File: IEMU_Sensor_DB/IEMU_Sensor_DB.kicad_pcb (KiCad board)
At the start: 2 copper layers, 51 x 29 mm, 12 parts, among them J1 USB_C_Receptacle_USB2.0_16P, J2 Conn_ARM_SWD_TagConnect_TC203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, J3 503398-1892, Q1 CSD85301Q2, U1 Ezurio BL54L15, U2 BQ29702DSER, U3 NPM1304-QEAA-R7, U4 USBLC6-2P6, U5 LSM6DSV320XTR, U6 MMC5603NJ

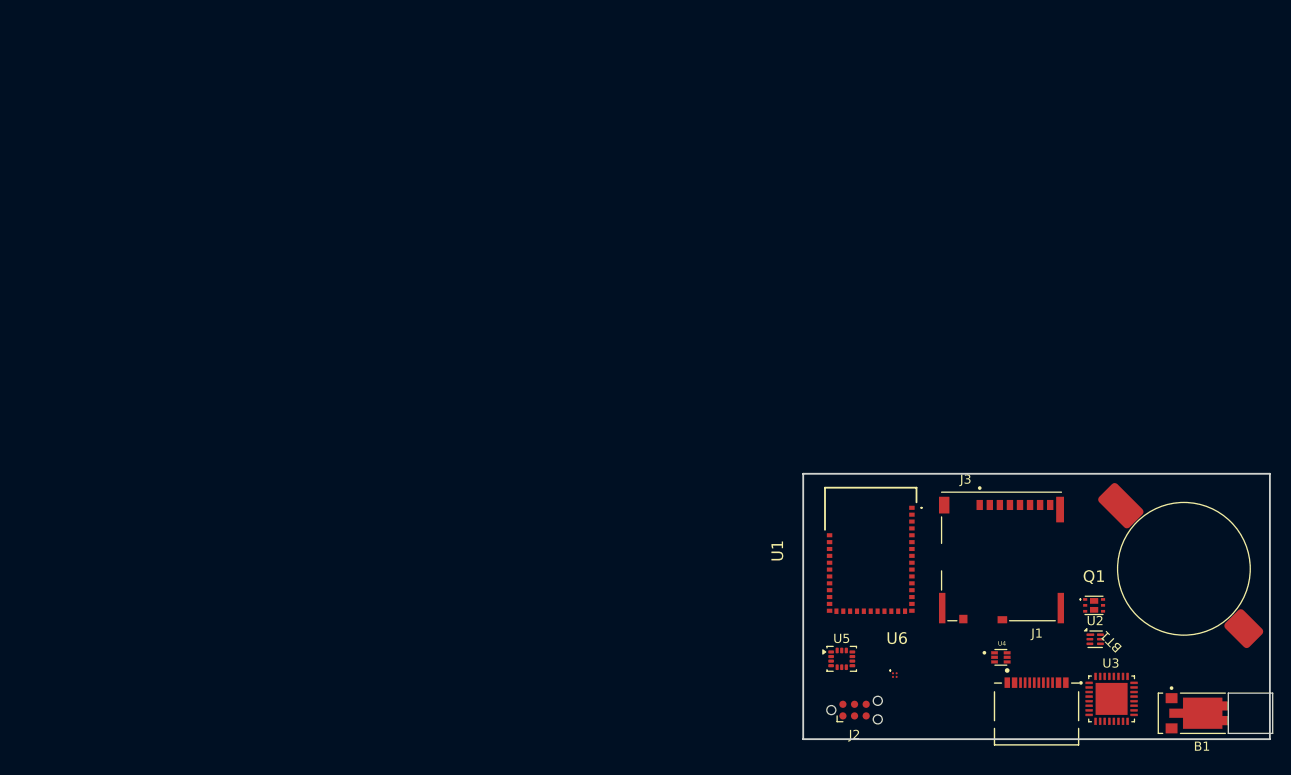
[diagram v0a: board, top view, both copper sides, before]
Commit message: created the layout for the sensor (not finished)
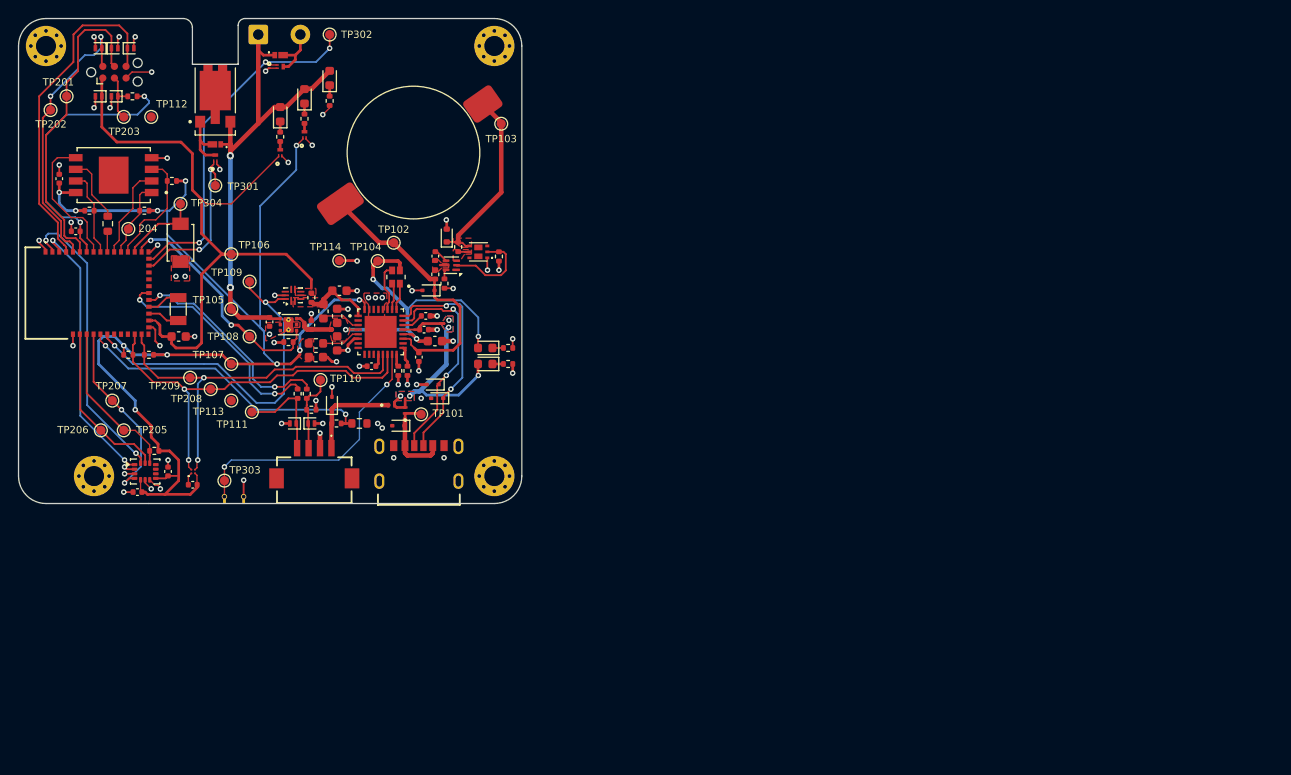
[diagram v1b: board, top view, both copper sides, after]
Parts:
- removed B1: VZ43FM1B8230001L, 0_Feedback:XDCR_VZ43FM1B8230001L
- removed BT1: Battery_Cell, 0_Power:CoinCell_LIR1455_LBY2
- removed J1: USB_C_Receptacle_USB2.0_16P, 0_Connectors:CONN_8p94X6p5X3p16_12L_GCC
- removed J2: Conn_ARM_SWD_TagConnect_TC2030-NL, Connector:Tag-Connect_TC2030-IDC-NL_2x03_P1.27mm_Vertical
- removed J3: 503398-1892, 0_Connectors:MOLEX_503398-1892
- removed Q1: CSD85301Q2, 0_Power:CSD85301Q2
- removed U1: Ezurio BL54L15, 0_MCU:BL54L15
- removed U2: BQ29702DSER, Package_SON:WSON-6_1.5x1.5mm_P0.5mm
- removed U3: NPM1304-QEAA-R7, 0_Power:QFN50P500X500X90-33N
- removed U4: USBLC6-2P6, 0_Power:SOT50P160X60-6N
- removed U5: LSM6DSV320XTR, Package_LGA:LGA-14_3x2.5mm_P0.5mm_LayoutBorder3x4y
- removed U6: MMC5603NJ, 0_Sensors:MMC5603NJ
- added 204: ~, TestPoint:TestPoint_Pad_D1.0mm, F.Cu at (101.2, 81.2)
- added BT101: Battery_Cell, 0_Power:CoinCell_LIR1455_LBY2, F.Cu at (138.6, 81.7)
- added C101: 1u, Capacitor_SMD:C_0402_1005Metric, F.Cu at (133.6, 92.2)
- added C102: 2u2, Capacitor_SMD:C_0402_1005Metric, F.Cu at (133.0, 95.2)
- added C103: 100n, Capacitor_SMD:C_0402_1005Metric, F.Cu at (134.8, 84.2)
- added C104: 100n, Capacitor_SMD:C_0402_1005Metric, F.Cu at (127.8, 96.2)
- added C105: 1u, Capacitor_SMD:C_0402_1005Metric, F.Cu at (133.8, 90.8)
- added C106: 10u, Capacitor_SMD:C_0603_1608Metric, F.Cu at (134.8, 93.5)
- added C107: 10u, Capacitor_SMD:C_0603_1608Metric, F.Cu at (124.1, 90.7)
- added C108: 10u, Capacitor_SMD:C_0603_1608Metric, F.Cu at (124.1, 93.7)
- added C109: 1u, Capacitor_SMD:C_0402_1005Metric, F.Cu at (121.2, 91.8)
- added C110: 1u, Capacitor_SMD:C_0402_1005Metric, F.Cu at (116.7, 91.4)
- added C111: 10u, Capacitor_SMD:C_0603_1608Metric, F.Cu at (124.3, 88.0)
- added C112: 10u, Capacitor_SMD:C_0603_1608Metric, F.Cu at (121.8, 95.2)
- added C201: 10u, Capacitor_SMD:C_0603_1608Metric, F.Cu at (106.8, 93.0)
- added C202: 3p7, Capacitor_SMD:C_0402_1005Metric, F.Cu at (95.5, 81.5)
- added C203: 100n, Capacitor_SMD:C_0402_1005Metric, F.Cu at (93.7, 75.8)
- added C204: 100n, Capacitor_SMD:C_0402_1005Metric, F.Cu at (105.6, 107.8)
- added C205: 100n, Capacitor_SMD:C_0402_1005Metric, F.Cu at (102.2, 110.0)
- added C206: 2u2, Capacitor_SMD:C_0402_1005Metric, F.Cu at (108.3, 109.2)
- added D101: ESD5Z5.0T1G, Diode_SMD:D_SOD-523_1, F.Cu at (130.8, 102.8)
- added D102: ESD5Z5.0T1G, Diode_SMD:D_SOD-523_1, F.Cu at (134.5, 98.2)
- added D103: ESD5Z5.0T1G, Diode_SMD:D_SOD-523_1, F.Cu at (135.0, 99.8)
- added D104: PMEG3010ESBYL, 0_Power:DIODFN100X60X30-2N, F.Cu at (131.5, 101.1)
- added D105: PMEG3010ESBYL, 0_Power:DIODFN100X60X30-2N, F.Cu at (130.0, 100.5)
- added D106: ESD5Z5.0T1G, Diode_SMD:D_SOD-523_1, F.Cu at (123.5, 100.2)
- added D107: ESD9L1P8, Diode_SMD:D_SOD-882, F.Cu at (119.2, 102.5)
- added D108: ESD9L1P8, Diode_SMD:D_SOD-882, F.Cu at (121.2, 102.5)
- added D109: LTST-C19HE1WT, 0_Feedback:LED_LTST-C19HE1WT, F.Cu at (130.5, 86.5)
- added D110: ESD5Z5.0T1G, Diode_SMD:D_SOD-523_1, F.Cu at (134.0, 88.0)
- added D111: TPD1E10B06DYAR, Diode_SMD:D_SOD-523, F.Cu at (136.0, 82.0)
- added D201: ESD9L1P8, Diode_SMD:D_SOD-882, F.Cu at (99.8, 61.5)
- added D202: ESD9L1P8, Diode_SMD:D_SOD-882, F.Cu at (98.0, 61.5)
- added D203: ESD9L1P8, Diode_SMD:D_SOD-882, F.Cu at (101.5, 61.5)
- added D204: ESD9L1P8, Diode_SMD:D_SOD-882, F.Cu at (99.8, 66.8)
- added D205: ESD9L1P8, Diode_SMD:D_SOD-882, F.Cu at (98.0, 66.8)
- added D301: D_Schottky_2A_40V_0603, 0_Power:0603_DSN, F.Cu at (110.8, 72.0)
- added D302: D_Schottky_2A_40V_0603, 0_Power:0603_DSN, F.Cu at (117.8, 62.2)
- added D303: LTST-C191KRKT, 0_Feedback:LTST-C191KRKT, F.Cu at (117.8, 68.7)
- added D304: LTST-C191KRKT, 0_Feedback:LTST-C191KRKT, F.Cu at (120.5, 66.8)
- added D305: LTST-C191KRKT, 0_Feedback:LTST-C191KRKT, F.Cu at (123.2, 64.8)
- added D306: LTST-C191KRKT, 0_Feedback:LTST-C191KRKT, F.Cu at (140.2, 96.0)
- added D307: LTST-C191KRKT, 0_Feedback:LTST-C191KRKT, F.Cu at (140.2, 94.2)
- added J101: USB4125-GF-A, 0_Connectors:GCT_USB4125-GF-A_REVA2, F.Cu at (133.0, 108.0)
- added J102: DF13-4P-1.25H(21), 0_Connectors:DF13-4P-1.25H(21), F.Cu at (121.6, 108.7)
- added J201: Conn_ARM_SWD_TagConnect_TC2030-NL, Connector:Tag-Connect_TC2030-IDC-NL_2x03_P1.27mm_Vertical, F.Cu at (99.7, 64.1)
- added J301: Conn_01x02_Pin, Connector_Wire:SolderWire-0.5sqmm_1x02_P4.6mm_D0.9mm_OD2.1mm, F.Cu at (115.5, 60.0)
- added L101: 2u2, Inductor_SMD:L_0603_1608Metric, F.Cu at (122.6, 90.2)
- added L102: 2u2, Inductor_SMD:L_0603_1608Metric, F.Cu at (121.8, 93.8)
- added M401: VZ43FM1B8230001L, 0_Feedback:XDCR_VZ43FM1B8230001L, F.Cu at (110.8, 67.0)
- added MH301: MountingHole_Pad, MountingHole:MountingHole_2.2mm_M2_Pad_Via, F.Cu at (97.5, 108.2)
- added MH302: MountingHole_Pad, MountingHole:MountingHole_2.2mm_M2_Pad_Via, F.Cu at (92.2, 61.2)
- added MH303: MountingHole_Pad, MountingHole:MountingHole_2.2mm_M2_Pad_Via, F.Cu at (141.2, 61.2)
- added MH304: MountingHole_Pad, MountingHole:MountingHole_2.2mm_M2_Pad_Via, F.Cu at (141.2, 108.2)
- added Q101: CSD85301Q2, 0_Power:CSD85301Q2, F.Cu at (139.5, 83.8)
- added Q301: CSD13381F4, 0_Power:DFN100X60X35-3N, F.Cu at (110.8, 73.5)
- added Q302: CSD13381F4, 0_Power:DFN100X60X35-3N, F.Cu at (117.8, 63.5)
- added Q303: CSD13381F4, 0_Power:DFN100X60X35-3N, F.Cu at (117.8, 72.9)
- added Q304: CSD13381F4, 0_Power:DFN100X60X35-3N, F.Cu at (120.5, 71.0)
- added R101: 10k, Resistor_SMD:R_0402_1005Metric, F.Cu at (121.2, 101.0)
- added R102: 47k, Resistor_SMD:R_0402_1005Metric, F.Cu at (131.8, 96.8)
- added R103: 47k, Resistor_SMD:R_0402_1005Metric, F.Cu at (130.8, 96.8)
- added R104: 330, Resistor_SMD:R_0402_1005Metric, F.Cu at (134.8, 86.2)
- added R105: 5M1, Resistor_SMD:R_0402_1005Metric, F.Cu at (137.3, 83.2)
- added R106: 5M1, Resistor_SMD:R_0402_1005Metric, F.Cu at (141.8, 84.2)
- added R107: 2k2, Resistor_SMD:R_0402_1005Metric, F.Cu at (135.8, 87.2)
- added R108: R_Shunt_1R, Resistor_SMD:R_0402_1005Metric, F.Cu at (121.2, 88.8)
- added R109: 1k, Resistor_SMD:R_0402_1005Metric, F.Cu at (119.8, 99.2)
- added R110: 1k, Resistor_SMD:R_0402_1005Metric, F.Cu at (120.8, 99.2)
- added R111: 510k, Resistor_SMD:R_0603_1608Metric, F.Cu at (126.5, 102.5)
- added R112: 1M, Resistor_SMD:R_0402_1005Metric, F.Cu at (124.0, 102.5)
- added R201: 1k, Resistor_SMD:R_0402_1005Metric, F.Cu at (101.7, 66.8)
- added R202: 22R, Resistor_SMD:R_0603_1608Metric, F.Cu at (99.0, 80.7)
- added R203: 47k, Resistor_SMD:R_0402_1005Metric, F.Cu at (97.0, 79.2)
- added R204: 47k, Resistor_SMD:R_0402_1005Metric, F.Cu at (106.0, 76.0)
- added R205: 47k, Resistor_SMD:R_0402_1005Metric, F.Cu at (103.0, 79.2)
- added R206: 10k, Resistor_SMD:R_0402_1005Metric, F.Cu at (104.1, 105.5)
- added R207: 2k2, Resistor_SMD:R_0402_1005Metric, F.Cu at (103.5, 95.0)
- added R208: 2k2, Resistor_SMD:R_0402_1005Metric, F.Cu at (101.2, 95.0)
- added R209: 1M, Resistor_SMD:R_0402_1005Metric, F.Cu at (118.8, 93.6)
- added R301: 330R, Resistor_SMD:R_0402_1005Metric, F.Cu at (117.8, 71.2)
- added R302: 330R, Resistor_SMD:R_0402_1005Metric, F.Cu at (120.5, 69.2)
- added R303: 330R, Resistor_SMD:R_0402_1005Metric, F.Cu at (123.2, 67.2)
- added R304: 1k, Resistor_SMD:R_0402_1005Metric, F.Cu at (142.8, 96.0)
- added R305: 1k, Resistor_SMD:R_0402_1005Metric, F.Cu at (142.8, 94.2)
- added SW301: NANOT_160_BP, 0_Feedback:NANOT160BP, F.Cu at (112.8, 111.0)
- added SW302: TS-1088-AR02016, 0_Feedback:SW_TS-1088-AR02016, F.Cu at (107.0, 82.8)
- added TP101: ~, TestPoint:TestPoint_Pad_D1.0mm, F.Cu at (133.2, 101.5)
- added TP102: ~, TestPoint:TestPoint_Pad_D1.0mm, F.Cu at (130.2, 82.8)
- added TP103: ~, TestPoint:TestPoint_Pad_D1.0mm, F.Cu at (142.0, 69.8)
- added TP104: ~, TestPoint:TestPoint_Pad_D1.0mm, F.Cu at (128.5, 84.8)
- added TP105: ~, TestPoint:TestPoint_Pad_D1.0mm, F.Cu at (112.5, 90.0)
- added TP106: ~, TestPoint:TestPoint_Pad_D1.0mm, F.Cu at (112.5, 84.0)
- added TP107: ~, TestPoint:TestPoint_Pad_D1.0mm, F.Cu at (112.5, 96.0)
- added TP108: ~, TestPoint:TestPoint_Pad_D1.0mm, F.Cu at (114.5, 93.0)
- added TP109: ~, TestPoint:TestPoint_Pad_D1.0mm, F.Cu at (114.5, 87.0)
- added TP110: ~, TestPoint:TestPoint_Pad_D1.0mm, F.Cu at (122.2, 97.8)
- added TP111: ~, TestPoint:TestPoint_Pad_D1.0mm, F.Cu at (114.8, 101.2)
- added TP112: ~, TestPoint:TestPoint_Pad_D1.0mm, F.Cu at (103.8, 69.0)
- added TP113: ~, TestPoint:TestPoint_Pad_D1.0mm, F.Cu at (112.5, 100.0)
- added TP114: ~, TestPoint:TestPoint_Pad_D1.0mm, F.Cu at (124.3, 84.7)
- added TP201: ~, TestPoint:TestPoint_Pad_D1.0mm, F.Cu at (94.5, 66.8)
- added TP202: ~, TestPoint:TestPoint_Pad_D1.0mm, F.Cu at (92.8, 68.2)
- added TP203: ~, TestPoint:TestPoint_Pad_D1.0mm, F.Cu at (100.8, 69.0)
- added TP205: ~, TestPoint:TestPoint_Pad_D1.0mm, F.Cu at (100.8, 103.2)
- added TP206: ~, TestPoint:TestPoint_Pad_D1.0mm, F.Cu at (98.2, 103.2)
- added TP207: ~, TestPoint:TestPoint_Pad_D1.0mm, F.Cu at (99.5, 100.0)
- added TP208: ~, TestPoint:TestPoint_Pad_D1.0mm, F.Cu at (110.2, 98.8)
- added TP209: ~, TestPoint:TestPoint_Pad_D1.0mm, F.Cu at (108.0, 97.5)
- added TP301: ~, TestPoint:TestPoint_Pad_D1.0mm, F.Cu at (110.8, 76.5)
- added TP302: ~, TestPoint:TestPoint_Pad_D1.0mm, F.Cu at (123.2, 60.0)
- added TP303: ~, TestPoint:TestPoint_Pad_D1.0mm, F.Cu at (111.8, 108.8)
- added TP304: ~, TestPoint:TestPoint_Pad_D1.0mm, F.Cu at (107.0, 78.5)
- added U101: NPM1304-QEAA-R7, 0_Power:QFN50P500X500X90-33N, F.Cu at (128.8, 92.5)
- added U102: BQ29702DSER, Package_SON:WSON-6_1.5x1.5mm_P0.5mm, F.Cu at (136.5, 85.2)
- added U103: TLV75530PDRVR, Package_SON:WSON-6-1EP_2x2mm_P0.65mm_EP1x1.6mm_ThermalVias, F.Cu at (118.8, 91.7)
- added U104: INA216A2RSWR, Package_DFN_QFN:Texas_RSW0010A_UQFN-10_1.4x1.8mm_P0.4mm, F.Cu at (119.2, 88.5)
- added U201: Ezurio BL54L15, 0_MCU:BL54L15, F.Cu at (97.0, 88.2)
- added U202: W25N02JWZEIF, 0_Memory:IC_W25N04KVZEIR, F.Cu at (99.7, 75.4)
- added U203: LSM6DSV320XTR, Package_LGA:LGA-14_3x2.5mm_P0.5mm_LayoutBorder3x4y, F.Cu at (103.1, 107.8)
- added U204: MMC5603NJ, 0_Sensors:MMC5603NJ, F.Cu at (108.3, 107.8)
- added Y201: 32.768kHz, Crystal:Crystal_SMD_3215-2Pin_3.2x1.5mm, F.Cu at (106.7, 90.0)
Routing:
- net +1V8_Peripherals: track 0.00 -> 140.5 mm, vias 0 -> 11
- net +1V8_MCU: track 0.00 -> 70.8 mm
- net GND: track 0.00 -> 70.6 mm, vias 0 -> 64
- net +3V0: track 0.00 -> 55.3 mm, vias 0 -> 2
- net /1_Power/NPM_SCL: track 0.00 -> 44.8 mm, vias 0 -> 2
- net /1_Power/NPM_SDA: track 0.00 -> 43.3 mm, vias 0 -> 2
- net +VSYS: track 0.00 -> 43.0 mm, vias 0 -> 4
- net /2_nRF Module & NAND Flash + IMU + Magnetometer/ACTUATOR_EXTERNAL_EN: track 0.00 -> 39.5 mm, vias 0 -> 3
- net /1_Power/MCU_CURR_MON_COMP: track 0.00 -> 39.3 mm, vias 0 -> 2
- net /2_nRF Module & NAND Flash + IMU + Magnetometer/SWD_O: track 0.00 -> 36.9 mm
- net /2_nRF Module & NAND Flash + IMU + Magnetometer/SWD_CLK: track 0.00 -> 34.8 mm
- net /1_Power/5V_CHG_DET: track 0.00 -> 33.0 mm, vias 0 -> 2
- net /2_nRF Module & NAND Flash + IMU + Magnetometer/SPI_MISO_IMU: track 0.00 -> 32.4 mm, vias 0 -> 2
- net /2_nRF Module & NAND Flash + IMU + Magnetometer/SWD_IO: track 0.00 -> 31.4 mm, vias 0 -> 2
- net +VBAT: track 0.00 -> 30.4 mm
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- added copper zone on F.Cu, net +1V8_MCU
- added copper zone on F.Cu, net +1V8_Peripherals
- added copper zone on B.Cu, net +VBUS_IN
- added copper zone on F.Cu, net +VBUS_IN
- added copper zone on F.Cu, net +VSYS
- added copper zone on F.Cu, net /1_Power/BAT-
- added copper zone on F.Cu, net /1_Power/BAT_P_BAT
- added copper zone on F.Cu, net /1_Power/BAT_P_DOUT
- added copper zone on F.Cu, net /1_Power/NPM_VOUT1
- added copper zone on F.Cu, net GND
- added copper zone on In1.Cu, net GND
- added copper zone on In2.Cu, net GND
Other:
- board size 51 x 29 mm -> 55 x 53 mm
- copper layers 2 -> 4
- rule pad_to_mask_clearance: 0 -> 0.05

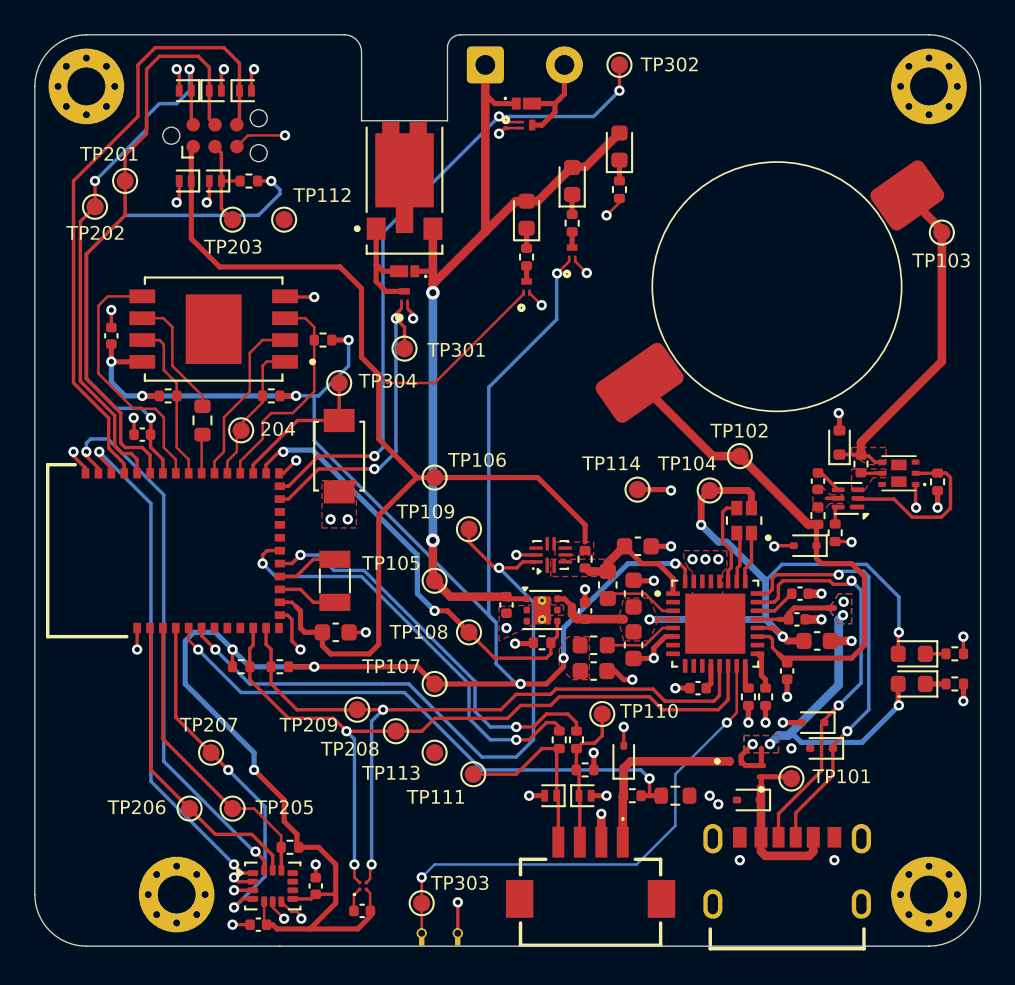
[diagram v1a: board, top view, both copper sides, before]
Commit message: finished layout for sensor
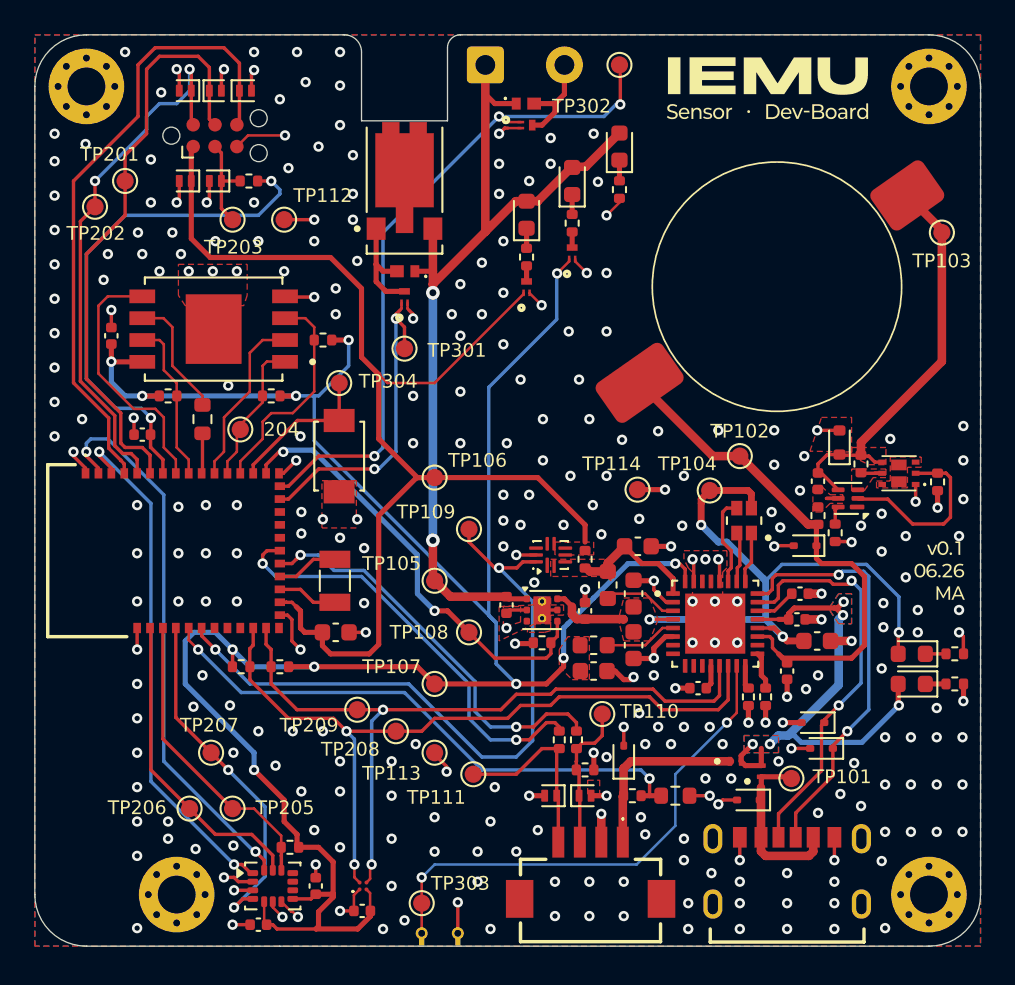
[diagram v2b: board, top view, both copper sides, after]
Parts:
- moved R202 0.08 mm to (99.0, 80.6)
- moved 204 0.07 mm to (101.2, 81.2)
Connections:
- net Net-(Q101-D1_1) renamed /1_Power/BAT_FET
- R202 pad 1: /2_nRF Module & NAND Flash + IMU + Magnetometer/QSPI_CLK -> /2_nRF Module & NAND Flash + IMU + Magnetometer/QSPI_CLK_MCU
- U201 pad 10: /2_nRF Module & NAND Flash + IMU + Magnetometer/QSPI_CLK -> /2_nRF Module & NAND Flash + IMU + Magnetometer/QSPI_CLK_MCU
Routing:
- net GND: track 70.6 -> 87.4 mm, vias 64 -> 301
- net /2_nRF Module & NAND Flash + IMU + Magnetometer/QSPI_CLK_MCU: track 0.00 -> 2.35 mm
- net /2_nRF Module & NAND Flash + IMU + Magnetometer/QSPI_CLK: track 9.46 -> 7.22 mm
- net /1_Power/BAT-: track 22.1 -> 24.1 mm
- net +VBUS_IN: track 27.3 -> 28.0 mm
- net /1_Power/BAT_P_COUT: track 10.1 -> 10.7 mm
- net (no net): vias 1 -> 0
- added copper zone on F.Cu, net /1_Power/BAT_FET
- added copper zone on B.Cu, net GND

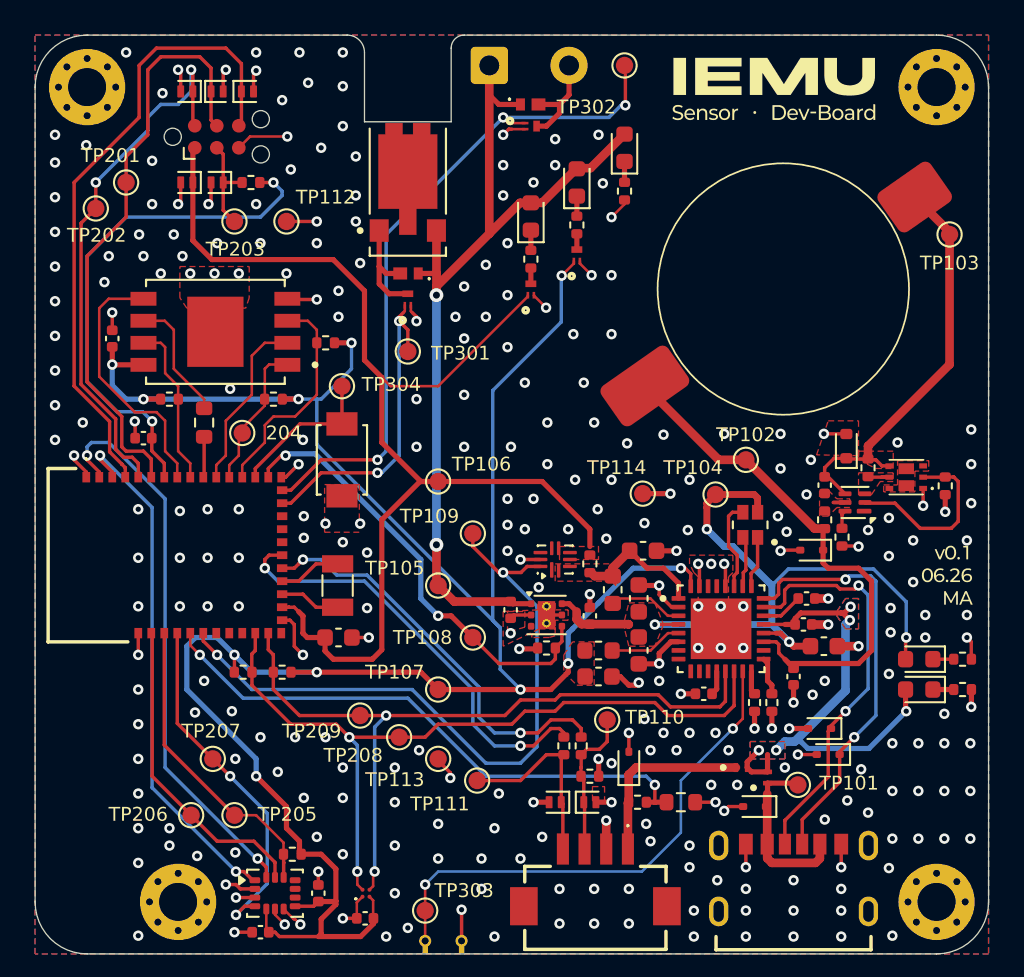
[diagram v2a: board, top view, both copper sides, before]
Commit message: layout of base and some fixes on the sensor layout
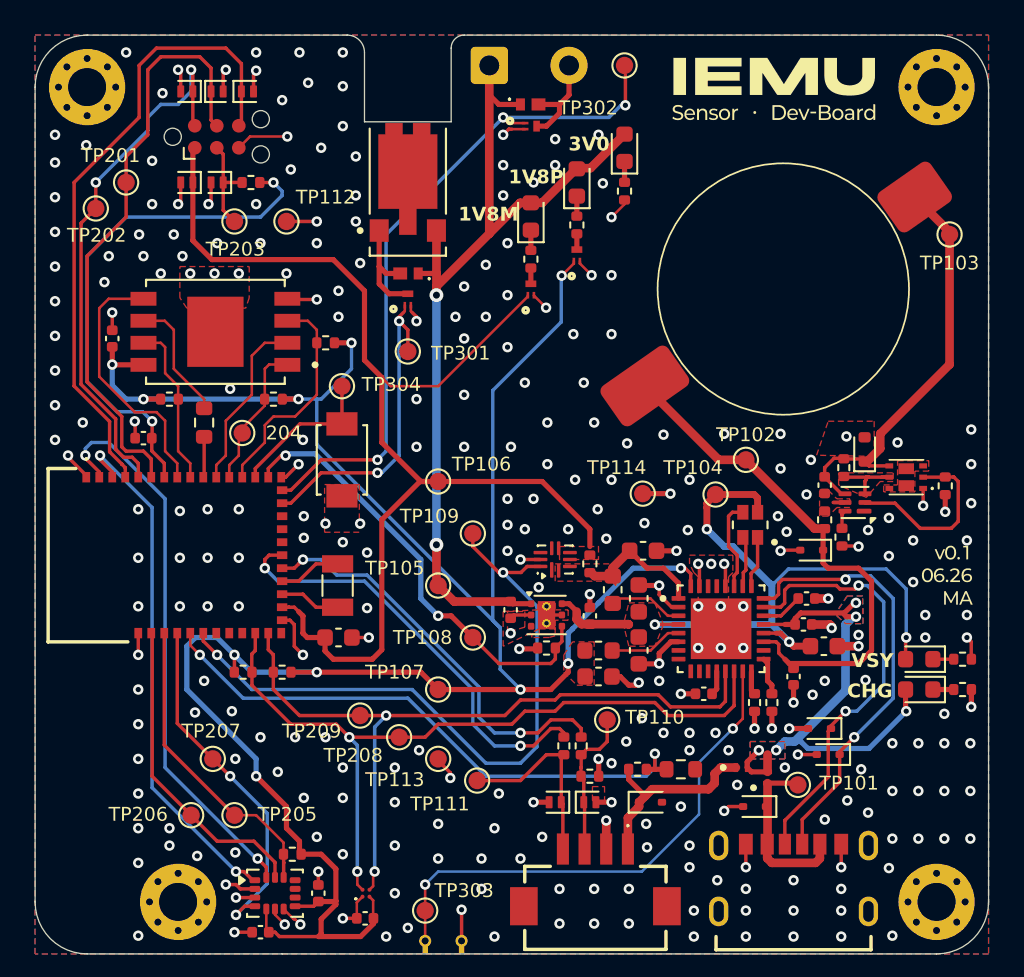
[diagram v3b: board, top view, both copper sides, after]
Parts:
- moved D106 2.57 mm to (124.8, 102.5), turned to 0 degrees
- moved R111 1.90 mm to (126.5, 100.6)
- moved R112 1.90 mm to (124.0, 100.6)
- moved R105 1.40 mm to (135.9, 83.2)
- moved D111 1.07 mm to (137.1, 82.2)
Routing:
- net GND: track 87.4 -> 84.3 mm, vias 301 -> 298
- net /1_Power/BAT_P_DOUT: track 1.64 -> 4.07 mm
- net /1_Power/CC1: track 23.7 -> 25.2 mm
- net +VBUS_IN_CONN: track 10.7 -> 11.6 mm
- net /1_Power/CC2: track 24.4 -> 25.3 mm
- net /1_Power/5V_CHG_DET: track 33.0 -> 33.7 mm
- net +VBUS_IN: track 28.0 -> 28.7 mm
- removed copper zone on F.Cu, net /1_Power/BAT-
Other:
- board text added: "1V8M"
- board text added: "1V8P"
- board text added: "3V0"
- board text added: "CHG"
- board text added: "VSY"
